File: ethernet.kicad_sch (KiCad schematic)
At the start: 0 parts

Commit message: Added barebones ethernet stuff and connectors
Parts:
- added T1: HR641680E, BR_Inductors:H1102FNL, symbol BR_Inductors:T_ARRAY_H1102FNL
- added U1: DP83825IRMQR, BR_IC:WQFN-24-3x3x0.8mm-DRV8311, symbol BR_IC_Ethernet:DP83825IRMQR
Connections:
- new net: T1.14, U1.10 (TD_N)
- new net: T1.16, U1.11 (TD_P)
- new net: T1.9, U1.7 (RD_N)
- new net: T1.11, U1.8 (RD_P)
- new net ETH.RX+: T1.6
- new net ETH.RX-: T1.8
- new net ETH.TX+: T1.1
- new net ETH.TX-: T1.3
- new net MAC.CRSDV: U1.20 (CRS_DV)
- new net MAC.MDC: U1.16 (MDC)
- new net MAC.MDIO: U1.15 (MDIO)
- new net MAC.RXD0: U1.18 (RX_D0)
- new net MAC.RXD1: U1.17 (RX_D1)
- new net MAC.RXER: U1.22 (RX_ER)
- new net MAC.TXD0: U1.23 (TX_D0)
- new net MAC.TXD1: U1.24 (TX_D1)
- new net MAC.TXEN: U1.1 (TX_EN)
- new net nRST: U1.5 (nRESET)

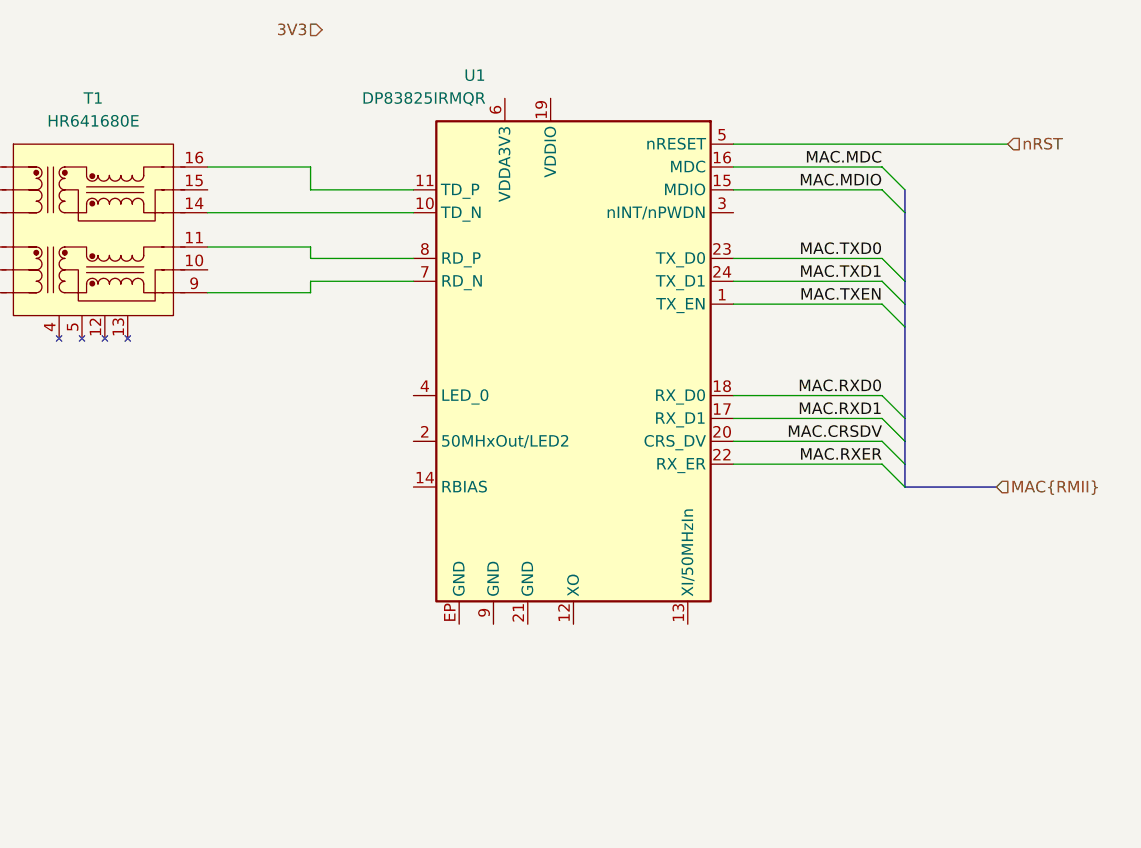
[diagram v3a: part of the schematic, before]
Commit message: rewiring STM32H563
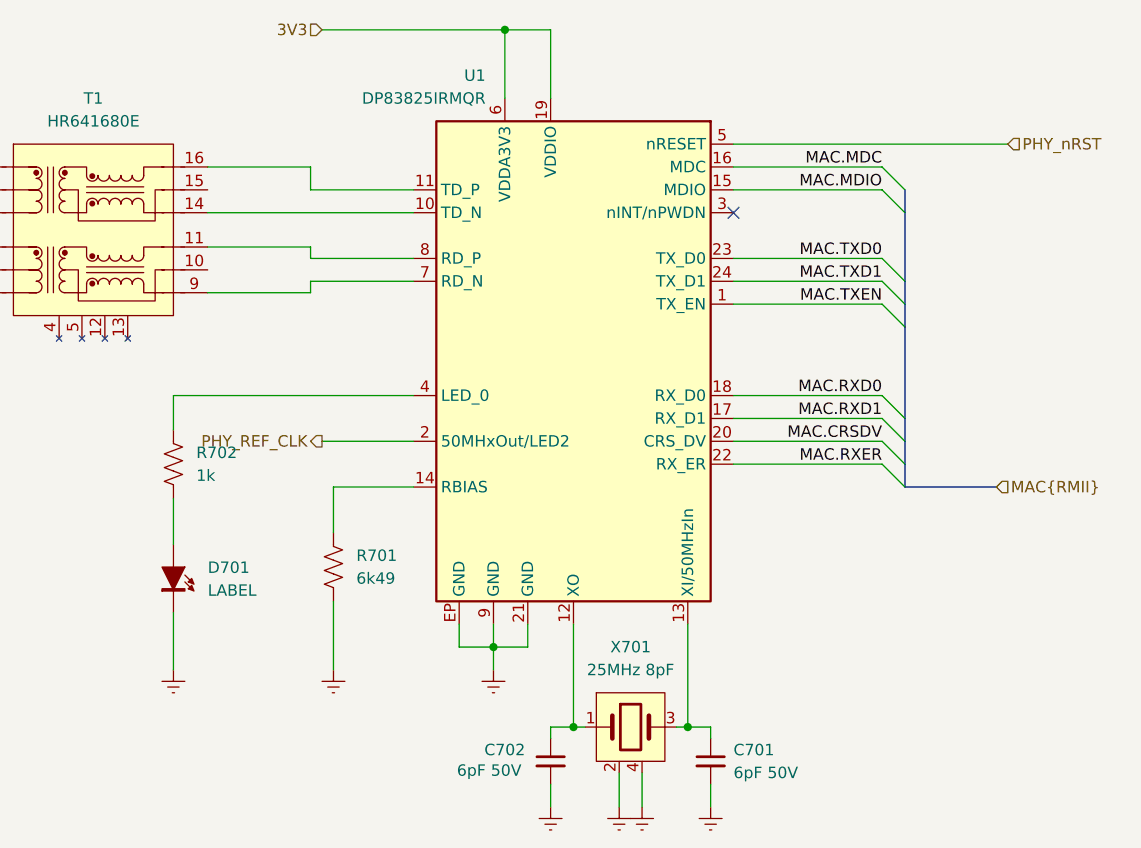
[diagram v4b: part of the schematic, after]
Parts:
- added C701, C702: 6pF 50V, BR_Passives:C_0201_0603Metric-minimized, symbol BR_Capacitors_0201:C_0201_6pF_50V_C0G_15%
- added D701: LABEL, BR_Optoelectronics:LED_0603_1608Metric, symbol BR_Optoelectronic:LTST-C191KGKT
- added R701: 6k49, BR_Passives:C_0402_1005Metric-minimized, symbol BR_Resistors_0402:R_0402_6k49
- added R702: 1k, BR_Passives:C_0402_1005Metric-minimized, symbol BR_Resistors_0402:R_0402_1k
- added X701: 25MHz 8pF, BR_Oscillators:Crystal_SMD_2016-4Pin_2.0x1.6mm, symbol BR_Oscillators:Xtal_NX2016SA-25MHZ
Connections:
- net 3V3: now also U1.19 (VDDIO), U1.6 (VDDA3V3)
- net at U1.12 (XO): now also C702.1, X701.1
- net at U1.13 (XI/50MHzIn): now also C701.1, X701.3
- net at U1.14 (RBIAS): now also R701.1
- net PHY_REF_CLK: now reaches U1.2 (50MHxOut/LED2)
- net GND: now reaches U1.21 (GND)
- net GND: now also U1.9 (GND), U1.EP (GND), C701.2, C702.2, D701.1 (K), R701.2, X701.2, X701.4
- net at U1.4 (LED_0): now also R702.1
- net nRST renamed PHY_nRST
- new net: D701.2 (A), R702.2
- no-connect marks 0 -> 1

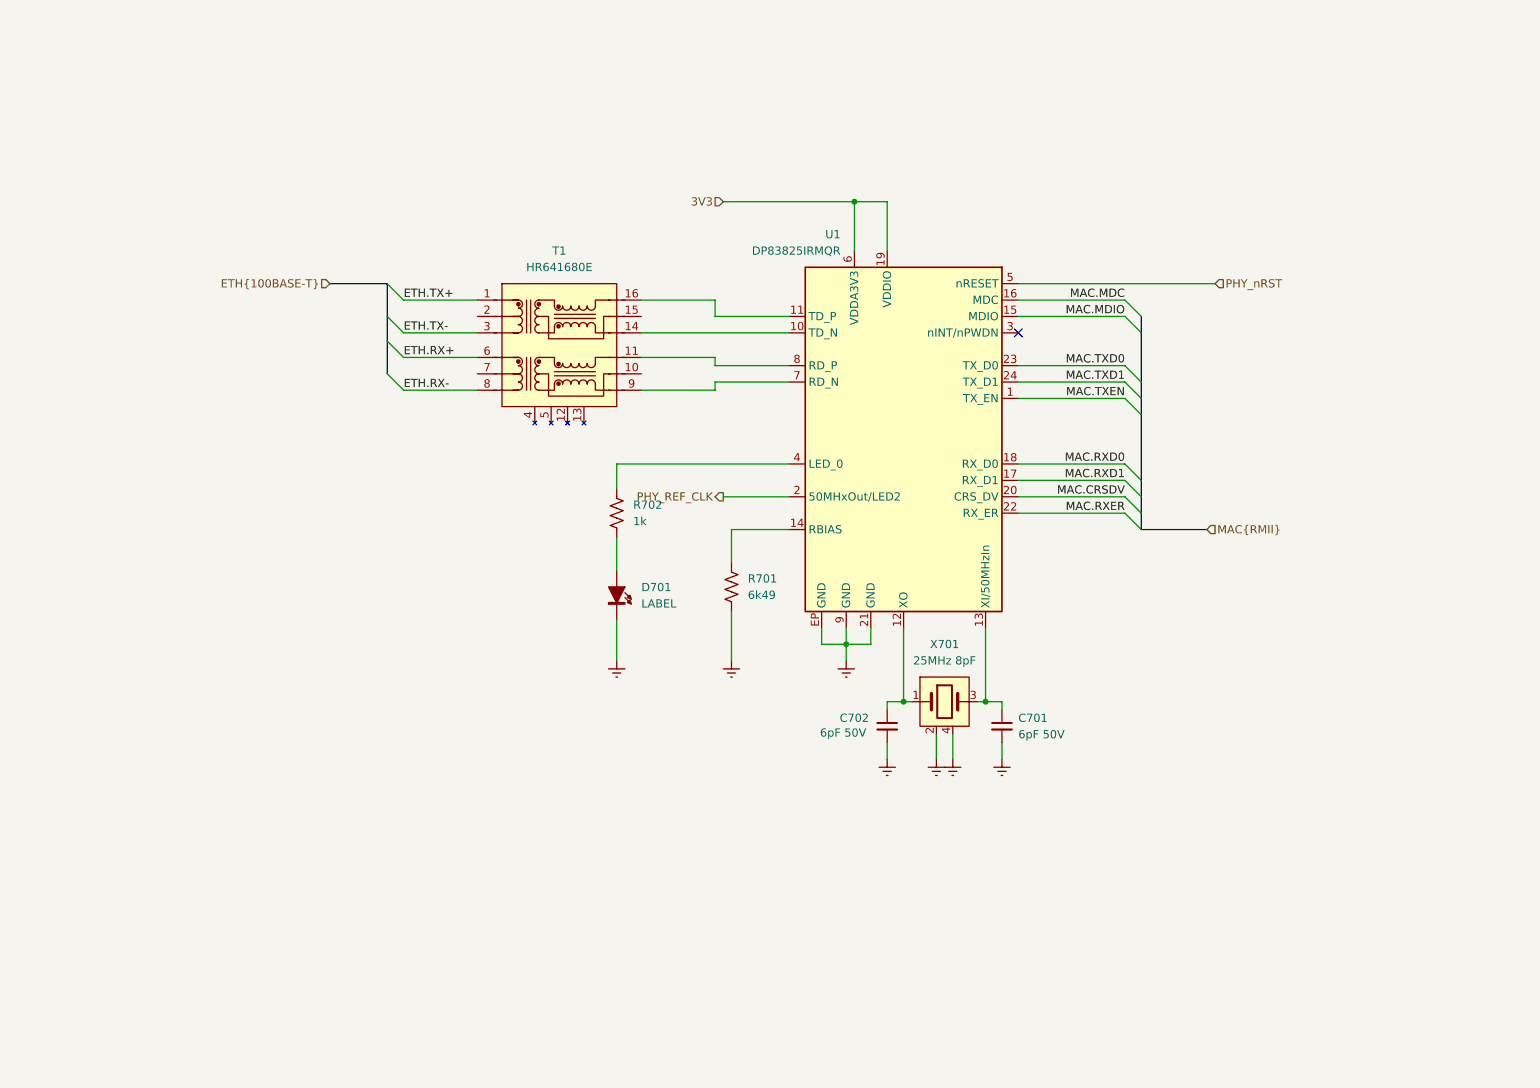
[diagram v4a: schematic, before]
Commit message: added rj45 and h-bridge + stm pinout spreadsheet
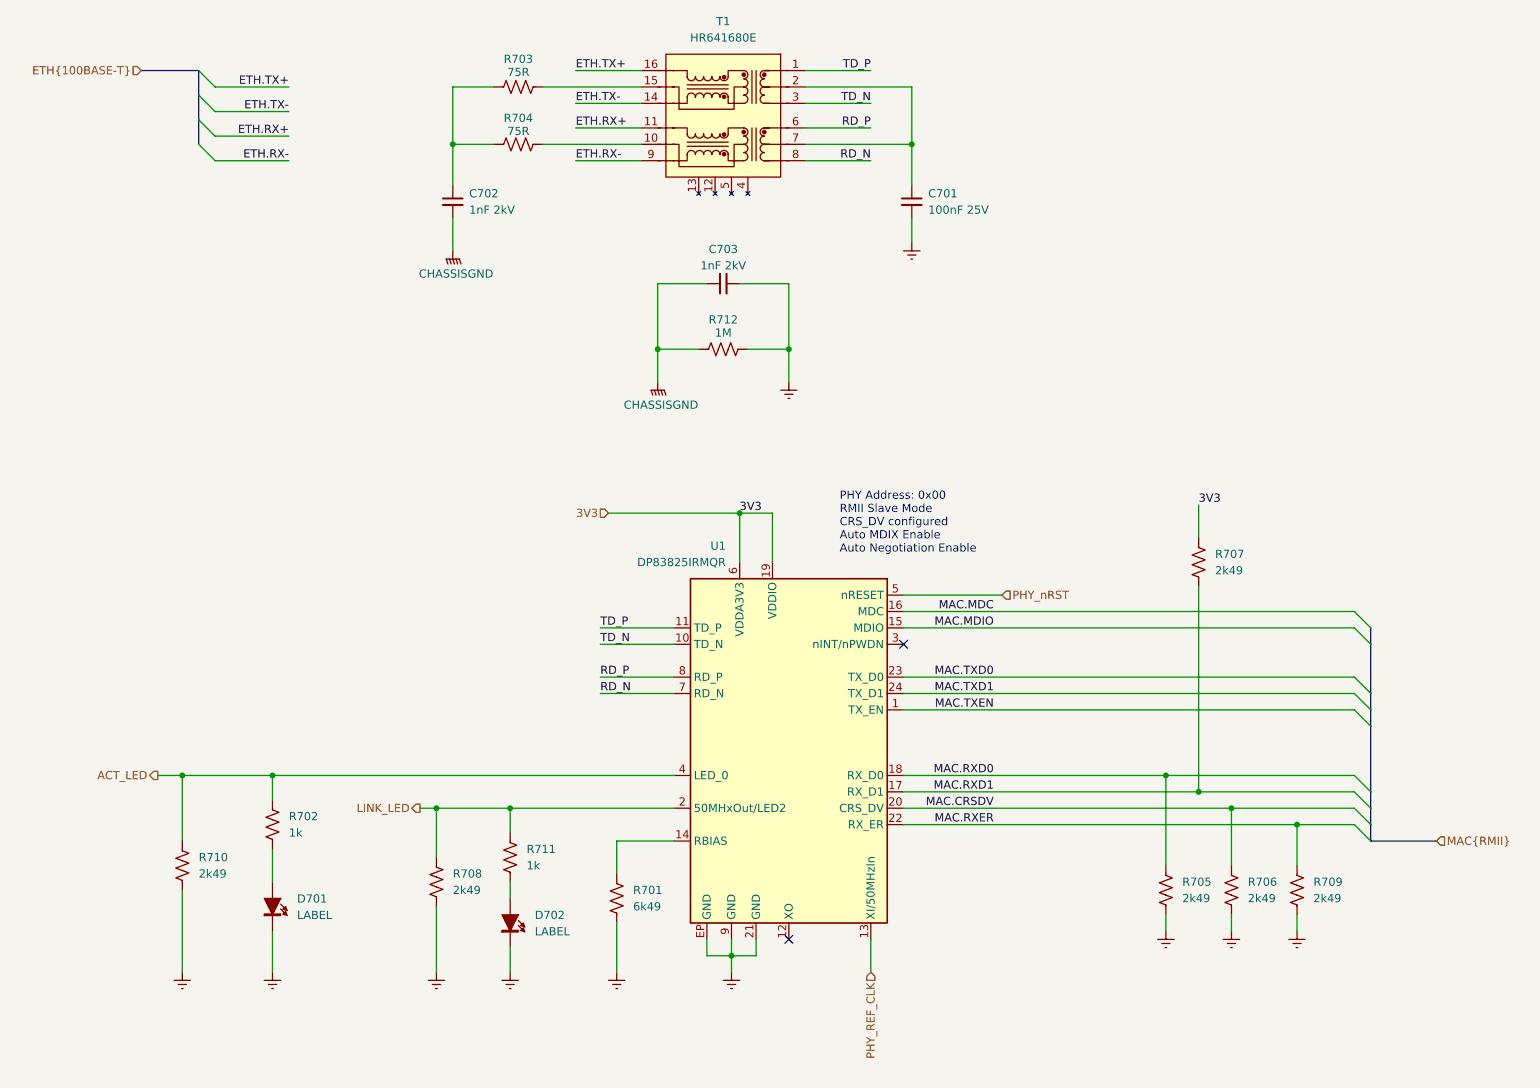
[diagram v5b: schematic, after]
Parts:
- removed C701, C702: 6pF 50V, BR_Passives:C_0201_0603Metric-minimized, symbol BR_Capacitors_0201:C_0201_6pF_50V_C0G_15%
- removed X701: 25MHz 8pF, BR_Oscillators:Crystal_SMD_2016-4Pin_2.0x1.6mm, symbol BR_Oscillators:Xtal_NX2016SA-25MHZ
- added C701: 100nF 25V, BR_Passives:C_0201_0603Metric-minimized, symbol BR_Capacitors_0201:C_0201_100nF_25V_X7R_10%
- added C702, C703: 1nF 2kV, BR_Passives:C_1206_3216Metric-minimized, symbol BR_Capacitors_1206:C_1206_1nF_2kV_X7R_10%
- added D702: LABEL, BR_Optoelectronics:LED_0603_1608Metric, symbol BR_Optoelectronic:LTST-C191KGKT
- added R703, R704: 75R, BR_Passives:C_0402_1005Metric-minimized, symbol BR_Resistors_0402:R_0402_75R
- added R705, R706, R707, R708, R709, R710: 2k49, BR_Passives:C_0402_1005Metric-minimized, symbol BR_Resistors_0402:R_0402_2k49
- added R711: 1k, BR_Passives:C_0402_1005Metric-minimized, symbol BR_Resistors_0402:R_0402_1k
- added R712: 1M, BR_Passives:C_0402_1005Metric-minimized, symbol BR_Resistors_0402:R_0402_1M
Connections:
- net 3V3: now also R707.1
- net ETH.RX+: now also T1.11; no longer T1.6
- net ETH.RX-: now also T1.9; no longer T1.8
- net ETH.TX+: now also T1.16; no longer T1.1
- net ETH.TX-: now also T1.14; no longer T1.3
- net GND: now also C701.2, C703.2, D702.1 (K), R705.2, R706.2, R708.2, R709.2, R710.2, R712.2
- net MAC.CRSDV: now also R706.1
- net MAC.RXD0: now also R705.1
- net MAC.RXD1: now also R707.2
- net MAC.RXER: now also R709.1
- net PHY_REF_CLK: now also U1.13 (XI/50MHzIn); no longer U1.2 (50MHxOut/LED2)
- net TD_N: now reaches U1.10 (TD_N)
- net TD_N: now also T1.3; no longer T1.14
- net TD_P: now reaches U1.11 (TD_P)
- net TD_P: now also T1.1; no longer T1.16
- net ACT_LED: now reaches R702.1, U1.4 (LED_0)
- net ACT_LED: now also R710.1
- net RD_N: now reaches U1.7 (RD_N)
- net RD_N: now also T1.8; no longer T1.9
- net RD_P: now reaches U1.8 (RD_P)
- net RD_P: now also T1.6; no longer T1.11
- net at T1.10: now also R704.2
- net at T1.15: now also R703.2
- net at T1.2: now also T1.7, C701.1
- new net: C702.1, R703.1, R704.1
- new net: D702.2 (A), R711.2
- new net CHASSISGND: C702.2, C703.1, R712.1
- new net LINK_LED: R708.1, R711.1, U1.2 (50MHxOut/LED2)
- no-connect marks 1 -> 2
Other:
- note added: "PHY Address: 0x00 RMII Slave Mode CRS_DV configured Auto MDIX Enable Auto Negotiation Enable"
- moved on the sheet: D701, R701, R702, T1, U1

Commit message: implementing feedback + added stepper driver
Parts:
- removed D701, D702: LABEL, BR_Optoelectronics:LED_0603_1608Metric, symbol BR_Optoelectronic:LTST-C191KGKT
- removed R702, R711: 1k, BR_Passives:C_0402_1005Metric-minimized, symbol BR_Resistors_0402:R_0402_1k
- added C704, C705: 10nF 25V, BR_Passives:C_0201_0603Metric-minimized, symbol BR_Capacitors_0201:C_0201_10nF_25V_X7R_10%
- added C706, C707: 100nF 25V, BR_Passives:C_0201_0603Metric-minimized, symbol BR_Capacitors_0201:C_0201_100nF_25V_X7R_10%
- added C708, C709, C712: 1uF 10V, BR_Passives:C_0402_1005Metric-minimized, symbol BR_Capacitors_0402:C_0402_1uF_10V_X7R_10%
- added C710, C711: 10uF 10V, BR_Passives:C_0402_1005Metric-minimized, symbol BR_Capacitors_0402:C_0402_10uF_10V_X5R_20%
- added R702: 30k, BR_Passives:C_0402_1005Metric-minimized, symbol BR_Resistors_0402:R_0402_30k
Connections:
- net 3V3: now also C704.1, C705.1, C706.1, C707.1, C708.1, C709.1, C710.1, C711.1, R702.2
- net GND: now also C704.2, C705.2, C706.2, C707.2, C708.2, C709.2, C710.2, C711.2, C712.2
- net PHY_nRST: now also C712.1, R702.1
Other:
- note added: "Capacitor charges to 1.7V (enables PSRAM) in ~10ms"
- moved on the sheet: C703, R712

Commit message: completed feedback from review + reannotated sheets
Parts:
- renumbered C710 to C701, C708 to C703, C706 to C704, C704 to C705, C705 to C706, C701 to C708, C712 to C710, C703 to C712, R710 to R701, R708 to R702, R701 to R705, R702 to R706, R712 to R707, R705 to R708, R707 to R709, R706 to R710, R709 to R711, T1 to T701, U1 to U701
